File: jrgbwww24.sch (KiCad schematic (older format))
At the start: 28 parts, among them J1 Srew_terminal, J2 Screw_Terminal_01x06, Q1 2N3904, Q10 IPA040N06N, Q2 2N3904, Q3 2N3904, Q4 IPA040N06N, Q5 IPA040N06N, Q6 IPA040N06N, Q7 2N3904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

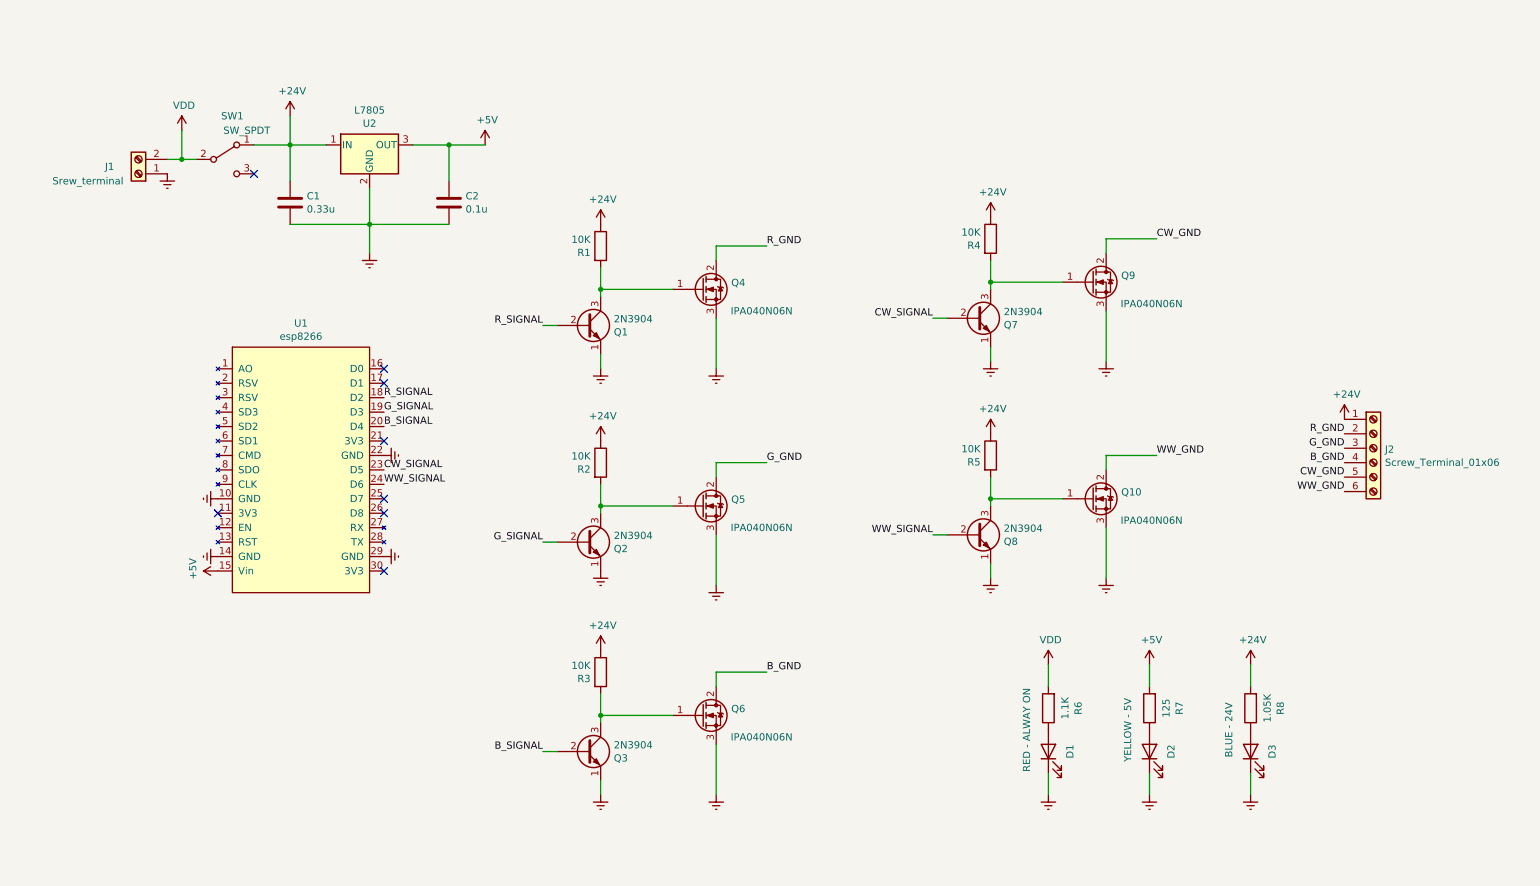
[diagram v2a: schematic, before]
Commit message: fixed footprints, schematics
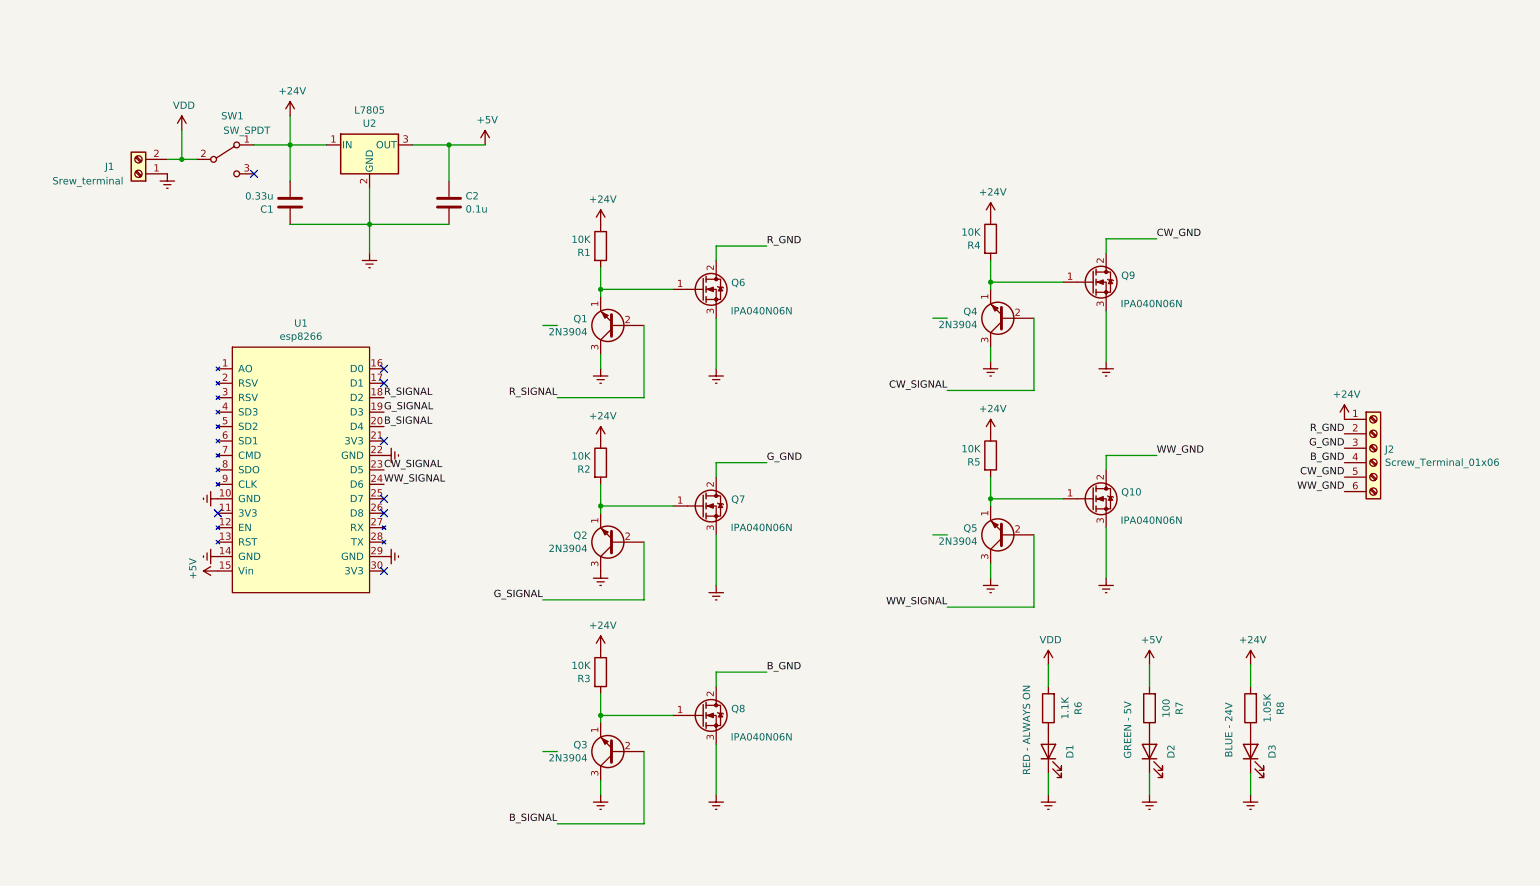
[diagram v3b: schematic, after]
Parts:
- D1: value RED - ALWAY ON -> RED - ALWAYS ON
- D2: value YELLOW - 5V -> GREEN - 5V
- R7: value 125 -> 100
- renumbered Q7 to Q4, Q8 to Q5, Q4 to Q6, Q5 to Q7, Q6 to Q8
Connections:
- wire segments 59 -> 68
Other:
- moved on the sheet: Q1, Q2, Q3, Q4, Q5
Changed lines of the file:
@@
 F 3 "~" H 2550 1900 50  0001 C CNN
 	1    2550 1900
-	-1   0    0    1
+	1    0    0    -1
 $EndComp
 $Comp
@@
 P 7800 5700
 F 0 "D1" H 7800 5550 50  0000 C CNN
-F 1 "RED - ALWAY ON" H 7950 5850 50  0000 C CNN
+F 1 "RED - ALWAYS ON" H 7950 5850 50  0000 C CNN
 F 2 "LED_SMD:LED_1206_3216Metric" H 7800 5700 50  0001 C CNN
 F 3 "~" H 7800 5700 50  0001 C CNN
@@
 L Transistor_BJT:2N3904 Q1
 U 1 1 6151569D
-P 4600 2750
-F 0 "Q1" H 4791 2704 50  0000 L CNN
-F 1 "2N3904" H 4791 2795 50  0000 L CNN
-F 2 "Package_TO_SOT_THT:TO-92_Inline" H 4800 2675 50  0001 L CIN
-F 3 "https://www.onsemi.com/pub/Collateral/2N3903-D.PDF" H 4600 2750 50  0001 L CNN
-	1    4600 2750
-	1    0    0    -1
+P 4800 2750
+F 0 "Q1" H 4991 2704 50  0000 L CNN
+F 1 "2N3904" H 4991 2795 50  0000 L CNN
+F 2 "Package_TO_SOT_THT:TO-92_Inline" H 5000 2675 50  0001 L CIN
+F 3 "https://www.onsemi.com/pub/Collateral/2N3903-D.PDF" H 4800 2750 50  0001 L CNN
+	1    4800 2750
+	-1   0    0    1
 $EndComp
 Wire Wire Line
@@
 Text Label 3200 3250 0    50   ~ 0
 R_SIGNAL
-Text Label 4300 2750 2    50   ~ 0
+Text Label 4400 3250 2    50   ~ 0
 R_SIGNAL
 Text Label 3200 3350 0    50   ~ 0
@@
 	4700 2950 4700 3050
 $Comp
-L library:IPA040N06N Q4
+L library:IPA040N06N Q6
 U 1 1 615156A7
 P 5400 2500
-F 0 "Q4" H 5604 2546 50  0000 L CNN
+F 0 "Q6" H 5604 2546 50  0000 L CNN
 F 1 "IPA040N06N" H 5600 2350 50  0000 L CNN
 F 2 "Package_TO_SOT_THT:TO-220F-3_Vertical" H 5600 2425 50  0001 L CIN
@@
 Wire Wire Line
 	5500 4200 5500 4550
-$Comp
-L Transistor_BJT:2N3904 Q2
-U 1 1 619CDCF5
-P 4600 4250
-F 0 "Q2" H 4791 4204 50  0000 L CNN
-F 1 "2N3904" H 4791 4295 50  0000 L CNN
-F 2 "Package_TO_SOT_THT:TO-92_Inline" H 4800 4175 50  0001 L CIN
-F 3 "https://www.onsemi.com/pub/Collateral/2N3903-D.PDF" H 4600 4250 50  0001 L CNN
-	1    4600 4250
-	1    0    0    -1
-$EndComp
-Wire Wire Line
-	4300 4250 4400 4250
-Text Label 4300 4250 2    50   ~ 0
+Text Label 4300 4650 2    50   ~ 0
 G_SIGNAL
 Text Label 5850 3700 0    50   ~ 0
@@
 	4700 4000 5200 4000
 $Comp
-L library:IPA040N06N Q5
+L library:IPA040N06N Q7
 U 1 1 619CDD0E
 P 5400 4000
-F 0 "Q5" H 5604 4046 50  0000 L CNN
+F 0 "Q7" H 5604 4046 50  0000 L CNN
 F 1 "IPA040N06N" H 5600 3850 50  0000 L CNN
 F 2 "Package_TO_SOT_THT:TO-220F-3_Vertical" H 5600 3925 50  0001 L CIN
@@
 L Transistor_BJT:2N3904 Q3
 U 1 1 61A5D465
-P 4600 5700
-F 0 "Q3" H 4791 5654 50  0000 L CNN
-F 1 "2N3904" H 4791 5745 50  0000 L CNN
-F 2 "Package_TO_SOT_THT:TO-92_Inline" H 4800 5625 50  0001 L CIN
-F 3 "https://www.onsemi.com/pub/Collateral/2N3903-D.PDF" H 4600 5700 50  0001 L CNN
-	1    4600 5700
-	1    0    0    -1
+P 4800 5700
+F 0 "Q3" H 4991 5654 50  0000 L CNN
+F 1 "2N3904" H 4991 5745 50  0000 L CNN
+F 2 "Package_TO_SOT_THT:TO-92_Inline" H 5000 5625 50  0001 L CIN
+F 3 "https://www.onsemi.com/pub/Collateral/2N3903-D.PDF" H 4800 5700 50  0001 L CNN
+	1    4800 5700
+	-1   0    0    1
 $EndComp
 Wire Wire Line
 	4300 5700 4400 5700
-Text Label 4300 5700 2    50   ~ 0
+Text Label 4400 6200 2    50   ~ 0
 B_SIGNAL
 Text Label 5850 5150 0    50   ~ 0
@@
 	4700 5900 4700 6000
 $Comp
-L library:IPA040N06N Q6
+L library:IPA040N06N Q8
 U 1 1 61A5D47E
 P 5400 5450
-F 0 "Q6" H 5604 5496 50  0000 L CNN
+F 0 "Q8" H 5604 5496 50  0000 L CNN
 F 1 "IPA040N06N" H 5600 5300 50  0000 L CNN
 F 2 "Package_TO_SOT_THT:TO-220F-3_Vertical" H 5600 5375 50  0001 L CIN
@@
 	8200 2650 8200 3000
 $Comp
-L Transistor_BJT:2N3904 Q7
+L Transistor_BJT:2N3904 Q4
 U 1 1 61A5D4AC
-P 7300 2700
-F 0 "Q7" H 7491 2654 50  0000 L CNN
-F 1 "2N3904" H 7491 2745 50  0000 L CNN
-F 2 "Package_TO_SOT_THT:TO-92_Inline" H 7500 2625 50  0001 L CIN
-F 3 "https://www.onsemi.com/pub/Collateral/2N3903-D.PDF" H 7300 2700 50  0001 L CNN
-	1    7300 2700
-	1    0    0    -1
+P 7500 2700
+F 0 "Q4" H 7691 2654 50  0000 L CNN
+F 1 "2N3904" H 7691 2745 50  0000 L CNN
+F 2 "Package_TO_SOT_THT:TO-92_Inline" H 7700 2625 50  0001 L CIN
+F 3 "https://www.onsemi.com/pub/Collateral/2N3903-D.PDF" H 7500 2700 50  0001 L CNN
+	1    7500 2700
+	-1   0    0    1
 $EndComp
 Wire Wire Line
 	7000 2700 7100 2700
-Text Label 7000 2700 2    50   ~ 0
+Text Label 7100 3200 2    50   ~ 0
 CW_SIGNAL
 Text Label 8550 2150 0    50   ~ 0
@@
 	8200 4150 8200 4500
 $Comp
-L Transistor_BJT:2N3904 Q8
+L Transistor_BJT:2N3904 Q5
 U 1 1 61A71ED6
-P 7300 4200
-F 0 "Q8" H 7491 4154 50  0000 L CNN
-F 1 "2N3904" H 7491 4245 50  0000 L CNN
-F 2 "Package_TO_SOT_THT:TO-92_Inline" H 7500 4125 50  0001 L CIN
-F 3 "https://www.onsemi.com/pub/Collateral/2N3903-D.PDF" H 7300 4200 50  0001 L CNN
-	1    7300 4200
-	1    0    0    -1
+P 7500 4200
+F 0 "Q5" H 7691 4154 50  0000 L CNN
+F 1 "2N3904" H 7691 4245 50  0000 L CNN
+F 2 "Package_TO_SOT_THT:TO-92_Inline" H 7700 4125 50  0001 L CIN
+F 3 "https://www.onsemi.com/pub/Collateral/2N3903-D.PDF" H 7500 4200 50  0001 L CNN
+	1    7500 4200
+	-1   0    0    1
 $EndComp
 Wire Wire Line
 	7000 4200 7100 4200
-Text Label 7000 4200 2    50   ~ 0
+Text Label 7100 4700 2    50   ~ 0
 WW_SIGNAL
 Text Label 8550 3650 0    50   ~ 0
@@
 P 8500 5700
 F 0 "D2" H 8500 5550 50  0000 C CNN
-F 1 "YELLOW - 5V" H 8650 5850 50  0000 C CNN
+F 1 "GREEN - 5V" H 8650 5850 50  0000 C CNN
 F 2 "LED_SMD:LED_1206_3216Metric" H 8500 5700 50  0001 C CNN
 F 3 "~" H 8500 5700 50  0001 C CNN
@@
 P 8500 5400
 F 0 "R7" V 8293 5400 50  0000 C CNN
-F 1 "125" V 8384 5400 50  0000 C CNN
+F 1 "100" V 8384 5400 50  0000 C CNN
 F 2 "Resistor_THT:R_Axial_DIN0207_L6.3mm_D2.5mm_P7.62mm_Horizontal" V 8430 5400 50  0001 C CNN
 F 3 "~" H 8500 5400 50  0001 C CNN
@@
 $EndComp
 $Comp
-L power:VDD #PWR?
+L power:VDD #PWR0102
 U 1 1 6170ACFF
 P 7800 5100
-F 0 "#PWR?" H 7800 4950 50  0001 C CNN
+F 0 "#PWR0102" H 7800 4950 50  0001 C CNN
 F 1 "VDD" H 7815 5273 50  0000 C CNN
 F 2 "" H 7800 5100 50  0001 C CNN
@@
 	1    0    0    -1
 $EndComp
+$Comp
+L Transistor_BJT:2N3904 Q2
+U 1 1 619CDCF5
+P 4800 4250
+F 0 "Q2" H 4991 4204 50  0000 L CNN
+F 1 "2N3904" H 4991 4295 50  0000 L CNN
+F 2 "Package_TO_SOT_THT:TO-92_Inline" H 5000 4175 50  0001 L CIN
+F 3 "https://www.onsemi.com/pub/Collateral/2N3903-D.PDF" H 4800 4250 50  0001 L CNN
+	1    4800 4250
+	-1   0    0    1
+$EndComp
+Wire Wire Line
+	5000 4250 5000 4650
+Wire Wire Line
+	5000 4650 4300 4650
+Wire Wire Line
+	5000 2750 5000 3250
+Wire Wire Line
+	5000 3250 4400 3250
+Wire Wire Line
+	7700 2700 7700 3200
+Wire Wire Line
+	7700 3200 7100 3200
+Wire Wire Line
+	7700 4200 7700 4700
+Wire Wire Line
+	7700 4700 7100 4700
+Wire Wire Line
+	5000 5700 5000 6200
+Wire Wire Line
+	5000 6200 4400 6200
 $EndSCHEMATC

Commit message: improved 5v, fan header
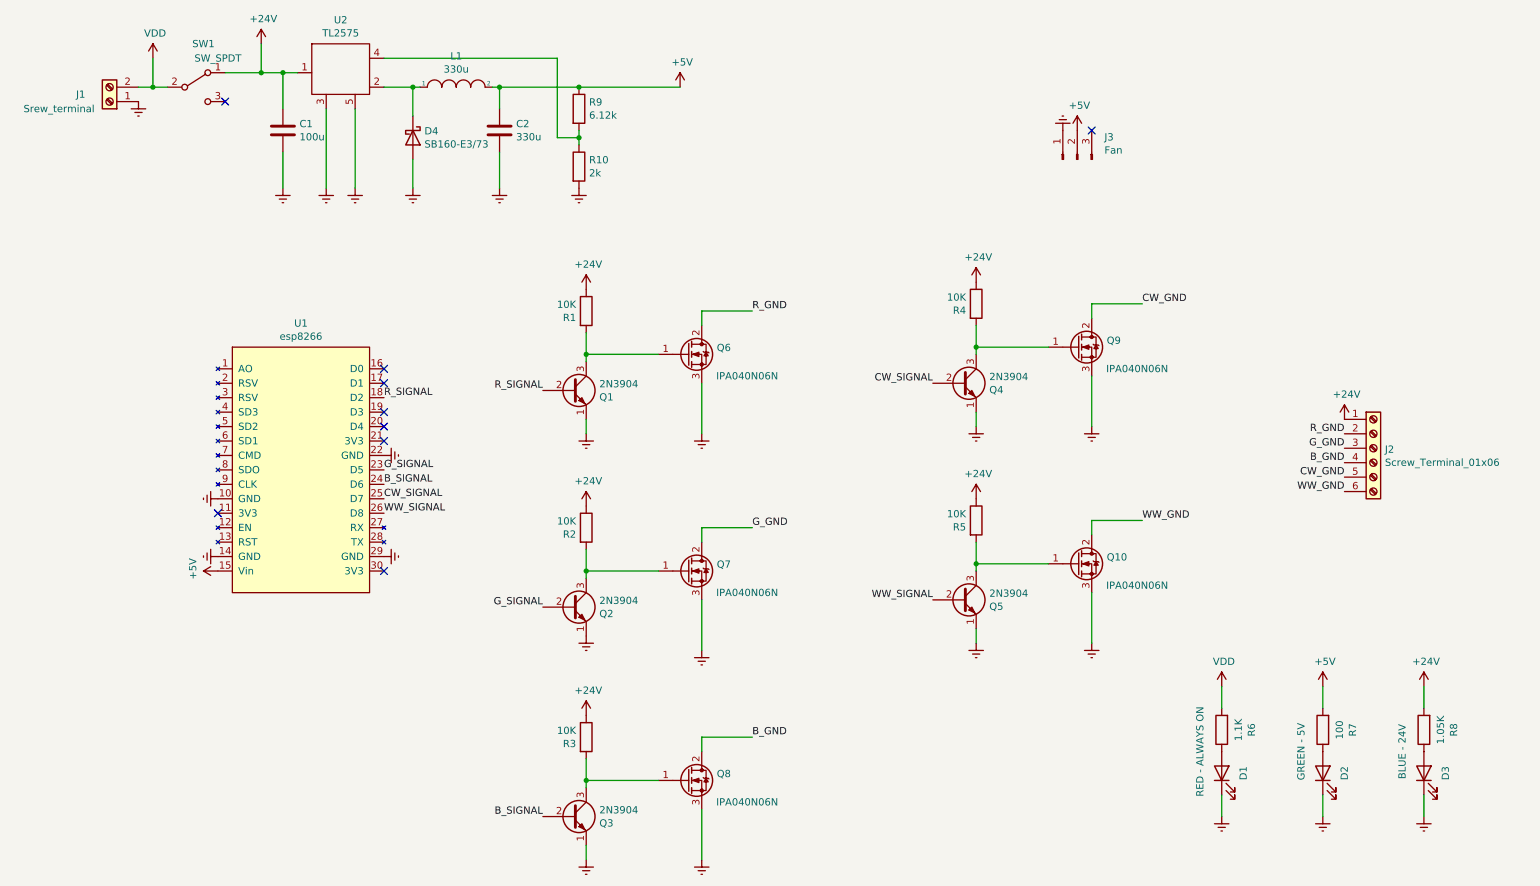
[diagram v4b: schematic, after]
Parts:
- removed U2: L7805, Package_TO_SOT_THT:TO-220-3_Horizontal_TabDown, symbol Regulator_Linear:L7805
- added D4: SB160-E3/73, Diode_THT:D_DO-41_SOD81_P7.62mm_Horizontal, symbol Device:D_Schottky
- added J3: Fan, Connector:FanPinHeader_1x03_P2.54mm_Vertical, symbol Connector:Conn_01x03_Male
- added L1: 330u, Inductor_SMD:L_Wuerth_WE-PD-Typ-LS_Handsoldering, symbol pspice:INDUCTOR
- added R10: 2k, Resistor_THT:R_Axial_DIN0207_L6.3mm_D2.5mm_P7.62mm_Horizontal, symbol Device:R
- added R9: 6.12k, Resistor_THT:R_Axial_DIN0207_L6.3mm_D2.5mm_P7.62mm_Horizontal, symbol Device:R
- added U2: TL2575, Package_TO_SOT_THT:TO-220-5_Horizontal_TabDown, symbol jrgbwww24:TL2575
- C1: value 0.33u -> 100u
- C2: value 0.1u -> 330u
- Q1, Q2, Q3, Q4, Q5: footprint Package_TO_SOT_THT:TO-92_Inline -> jrgbwww24:TO-92_Inline
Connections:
- wire segments 68 -> 65
- no-connect marks 8 -> 9
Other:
- moved on the sheet: D1, D2, D3, Q1, Q10, Q2, Q3, Q4, Q5, Q6, Q7, Q8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

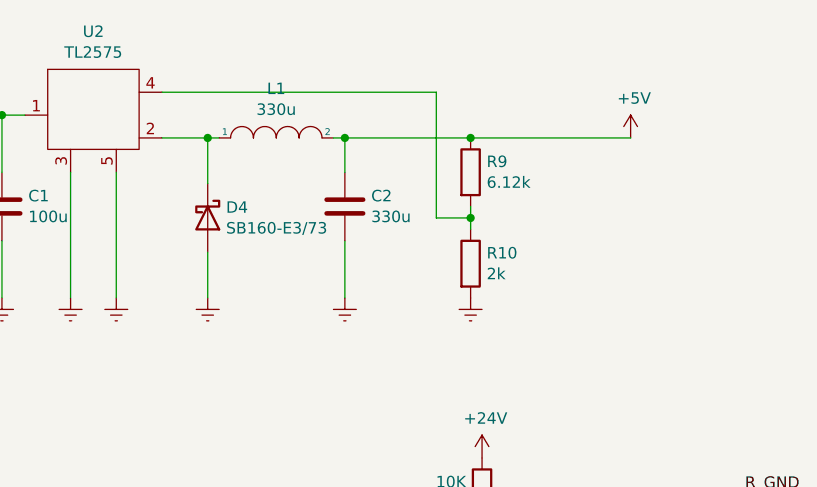
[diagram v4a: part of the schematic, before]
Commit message: fixed 5 v power supply
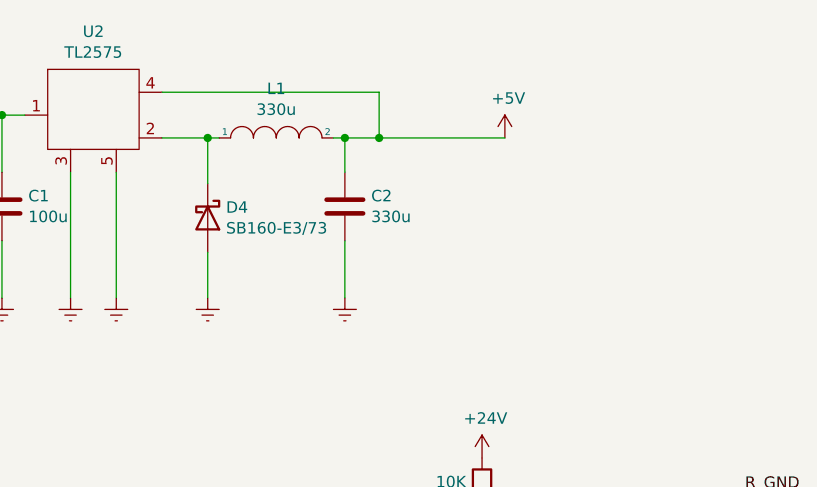
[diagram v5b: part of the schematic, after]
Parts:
- removed R10: 2k, Resistor_THT:R_Axial_DIN0207_L6.3mm_D2.5mm_P7.62mm_Horizontal, symbol Device:R
- removed R9: 6.12k, Resistor_THT:R_Axial_DIN0207_L6.3mm_D2.5mm_P7.62mm_Horizontal, symbol Device:R
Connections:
- net +5V: now also U2.4
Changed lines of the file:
@@
 L power:+5V #5V0101
 U 1 1 61923651
-P 5250 1100
-F 0 "#5V0101" H 5250 950 50  0001 C CNN
-F 1 "+5V" H 5265 1273 50  0000 C CNN
-F 2 "" H 5250 1100 50  0001 C CNN
-F 3 "" H 5250 1100 50  0001 C CNN
-	1    5250 1100
+P 4700 1100
+F 0 "#5V0101" H 4700 950 50  0001 C CNN
+F 1 "+5V" H 4715 1273 50  0000 C CNN
+F 2 "" H 4700 1100 50  0001 C CNN
+F 3 "" H 4700 1100 50  0001 C CNN
+	1    4700 1100
 	1    0    0    -1
 $EndComp
@@
 Wire Wire Line
 	4000 1800 4000 1550
-$Comp
-L Device:R R9
-U 1 1 6196CF2A
-P 4550 1250
-F 0 "R9" H 4620 1296 50  0000 L CNN
-F 1 "6.12k" H 4620 1205 50  0000 L CNN
-F 2 "Resistor_THT:R_Axial_DIN0207_L6.3mm_D2.5mm_P7.62mm_Horizontal" V 4480 1250 50  0001 C CNN
-F 3 "~" H 4550 1250 50  0001 C CNN
-	1    4550 1250
-	1    0    0    -1
-$EndComp
-$Comp
-L Device:R R10
-U 1 1 6196EC16
-P 4550 1650
-F 0 "R10" H 4620 1696 50  0000 L CNN
-F 1 "2k" H 4620 1605 50  0000 L CNN
-F 2 "Resistor_THT:R_Axial_DIN0207_L6.3mm_D2.5mm_P7.62mm_Horizontal" V 4480 1650 50  0001 C CNN
-F 3 "~" H 4550 1650 50  0001 C CNN
-	1    4550 1650
-	1    0    0    -1
-$EndComp
-Wire Wire Line
-	4550 1400 4550 1450
-Wire Wire Line
-	4550 1450 4400 1450
-Wire Wire Line
-	4400 1450 4400 900
-Connection ~ 4550 1450
-Wire Wire Line
-	4550 1450 4550 1500
-Connection ~ 4550 1100
-Wire Wire Line
-	4550 1100 5250 1100
+Connection ~ 4150 1100
 Wire Wire Line
 	4000 1250 4000 1100
@@
 Wire Wire Line
 	3400 1600 3400 1800
-$Comp
-L power:Earth #PWR0103
-U 1 1 619FB77A
-P 4550 1800
-F 0 "#PWR0103" H 4550 1550 50  0001 C CNN
-F 1 "Earth" H 4550 1650 50  0001 C CNN
-F 2 "" H 4550 1800 50  0001 C CNN
-F 3 "~" H 4550 1800 50  0001 C CNN
-	1    4550 1800
-	1    0    0    -1
-$EndComp
 $Comp
 L power:Earth #PWR0104
@@
 $EndComp
 Wire Wire Line
-	3200 900  4400 900
-Wire Wire Line
-	4000 1100 4550 1100
+	3200 900  4150 900
+Wire Wire Line
+	4000 1100 4150 1100
 Text Label 4300 4700 2    50   ~ 0
 G_SIGNAL
@@
 $EndComp
 NoConn ~ 8100 1400
+Wire Wire Line
+	4150 1100 4150 900
+Wire Wire Line
+	4150 1100 4700 1100
 $EndSCHEMATC
